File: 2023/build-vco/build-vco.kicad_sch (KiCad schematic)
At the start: 12 parts, among them M1 PMOS_OR1, M10 NMOS_OR1, M11 NMOS_OR1, M2 NMOS_OR1, M27 NMOS_OR1, M3 PMOS_OR1, M4 NMOS_OR1, M5 NMOS_OR1, M6 NMOS_OR1, M7 NMOS_OR1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

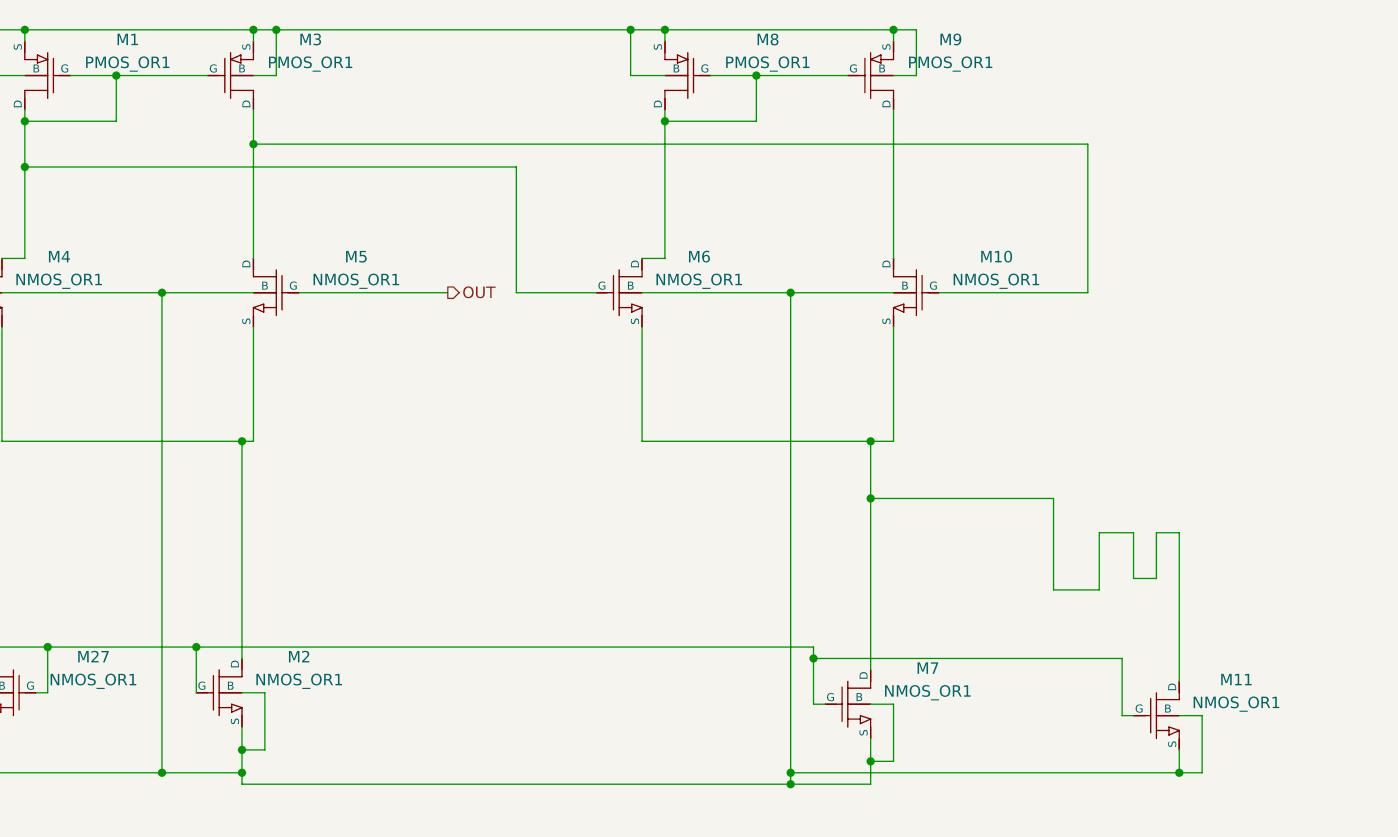
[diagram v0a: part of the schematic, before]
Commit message: DEBUG ポートを借り追加。LVS OK.
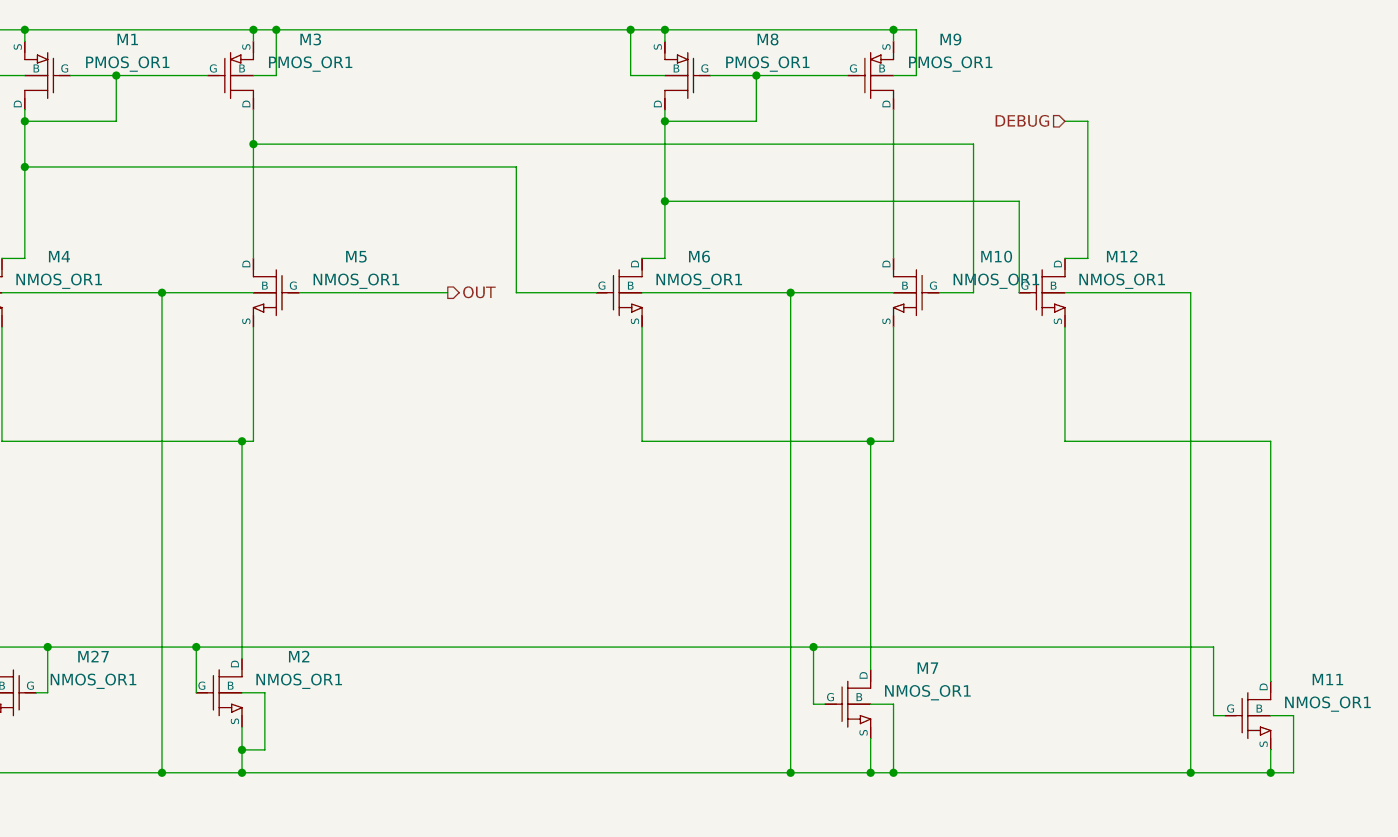
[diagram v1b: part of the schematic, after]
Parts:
- added M12: NMOS_OR1, symbol OR1Symbols:NMOS_OR1
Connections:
- net 0: now also M12.4 (B)
- net at M6.1 (D), M8.1 (D), M8.2 (G)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: now also M12.2 (G)
- net at M10.3 (S), M6.3 (S), M7.1 (D): no longer M11.1 (D)
- new net: M11.1 (D), M12.3 (S)
- new net DEBUG: M12.1 (D)
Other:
- moved on the sheet: M11

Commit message: 3段出来た。
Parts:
- added M13, M14: PMOS_OR1, symbol OR1Symbols:PMOS_OR1
- added M15: NMOS_OR1, symbol OR1Symbols:NMOS_OR1
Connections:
- net 0: now also M15.4 (B)
- net VDD: now also M13.3 (S), M13.4 (B), M14.3 (S), M14.4 (B)
- net at M10.1 (D), M9.1 (D): now also M15.2 (G)
- net at M11.1 (D), M12.3 (S): now also M15.3 (S)
- net DEBUG: no longer names the net of M12.1 (D)
- net DEBUG: now also M13.1 (D), M13.2 (G), M14.2 (G)
- new net: M14.1 (D), M15.1 (D)

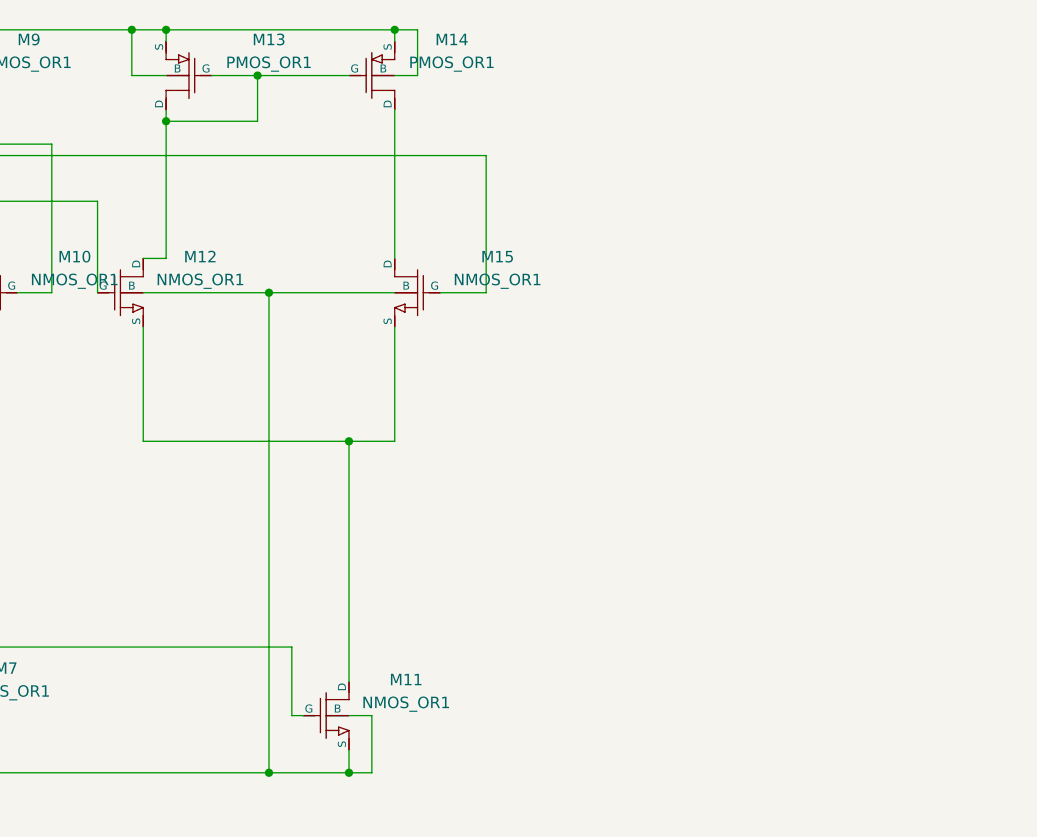
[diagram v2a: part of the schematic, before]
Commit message: 4段までOK. LVS OK.
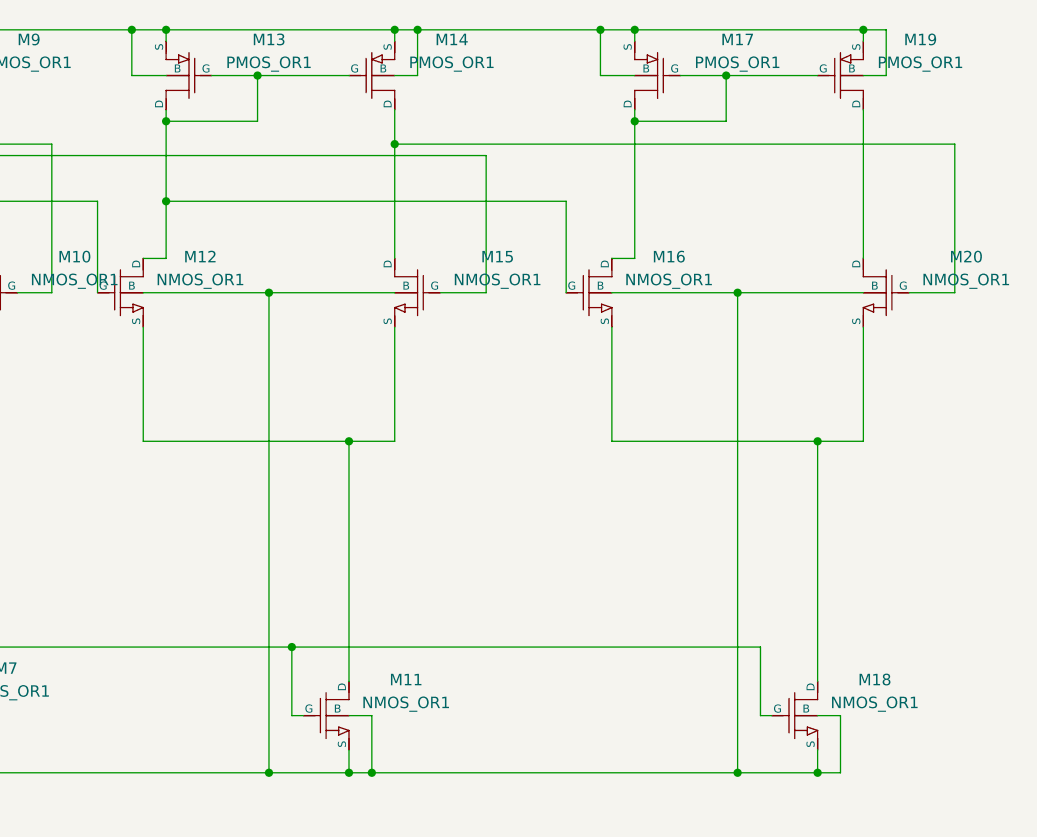
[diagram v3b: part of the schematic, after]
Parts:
- added M16, M18, M20: NMOS_OR1, symbol OR1Symbols:NMOS_OR1
- added M17, M19: PMOS_OR1, symbol OR1Symbols:PMOS_OR1
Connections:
- net 0: now also M16.4 (B), M18.3 (S), M18.4 (B), M20.4 (B)
- net IN: now also M18.2 (G)
- net VDD: now also M17.3 (S), M17.4 (B), M19.3 (S), M19.4 (B)
- net at M14.1 (D), M15.1 (D): now also M20.2 (G)
- net at M12.1 (D), M13.1 (D), M13.2 (G)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: now also M16.2 (G)
- new net: M16.1 (D), M17.1 (D), M17.2 (G), M19.2 (G)
- new net: M16.3 (S), M18.1 (D), M20.3 (S)
- new net: M19.1 (D), M20.1 (D)

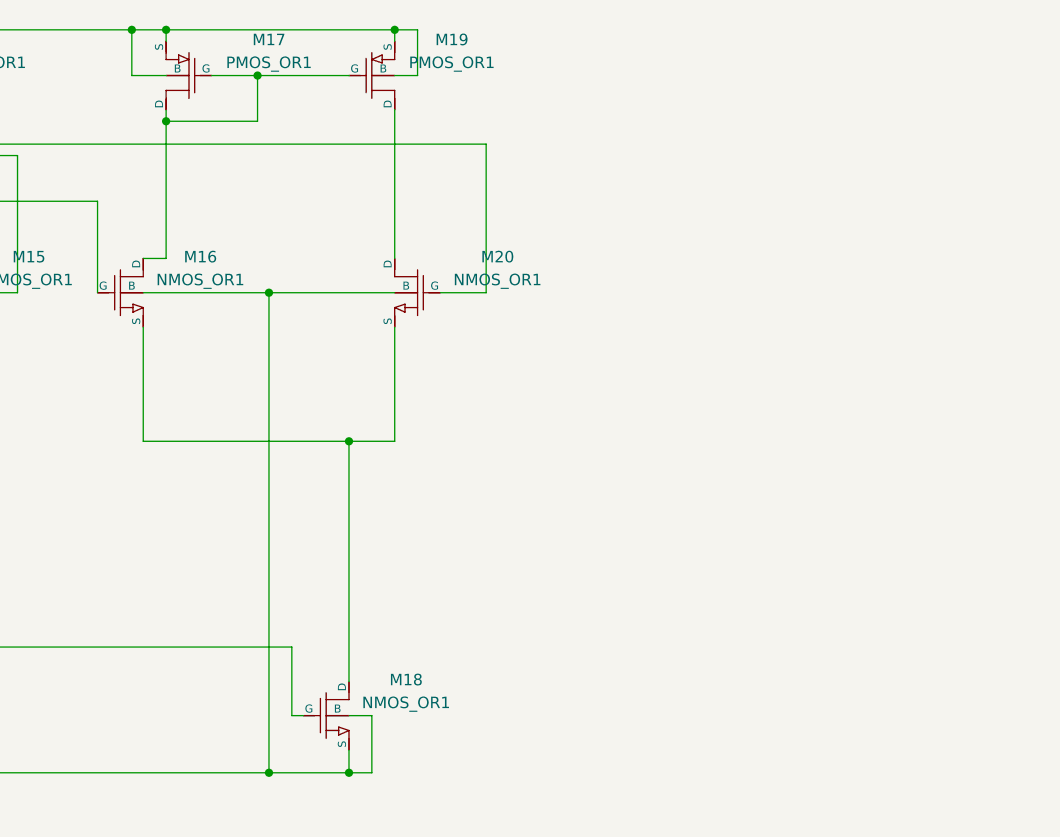
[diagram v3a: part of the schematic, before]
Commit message: 最終段の5段までOK. LVS OK.
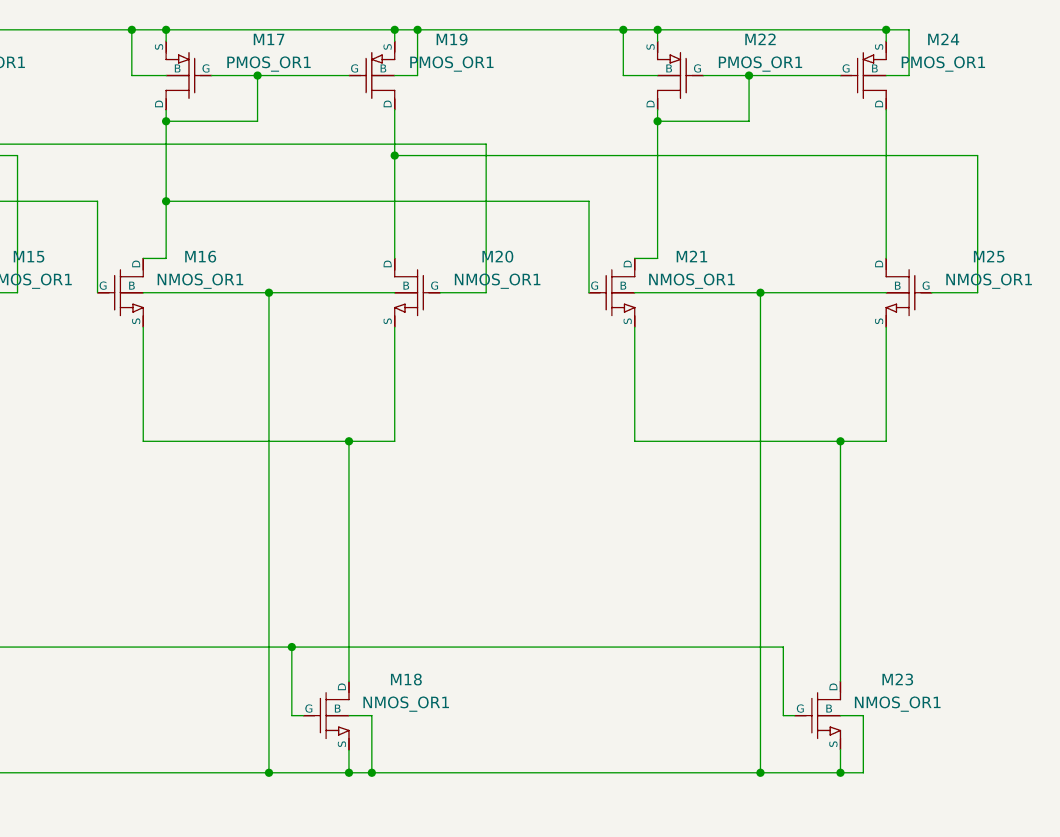
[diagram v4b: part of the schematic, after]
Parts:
- added M21, M23, M25: NMOS_OR1, symbol OR1Symbols:NMOS_OR1
- added M22, M24: PMOS_OR1, symbol OR1Symbols:PMOS_OR1
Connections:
- net 0: now also M21.4 (B), M23.3 (S), M23.4 (B), M25.4 (B)
- net IN: now also M23.2 (G)
- net VDD: now also M22.3 (S), M22.4 (B), M24.3 (S), M24.4 (B)
- net at M16.1 (D), M17.1 (D), M17.2 (G)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: now also M21.2 (G)
- net at M19.1 (D), M20.1 (D): now also M25.2 (G)
- new net: M24.1 (D), M25.1 (D)
- new net: M21.1 (D), M22.1 (D), M22.2 (G), M24.2 (G)
- new net: M21.3 (S), M23.1 (D), M25.3 (S)

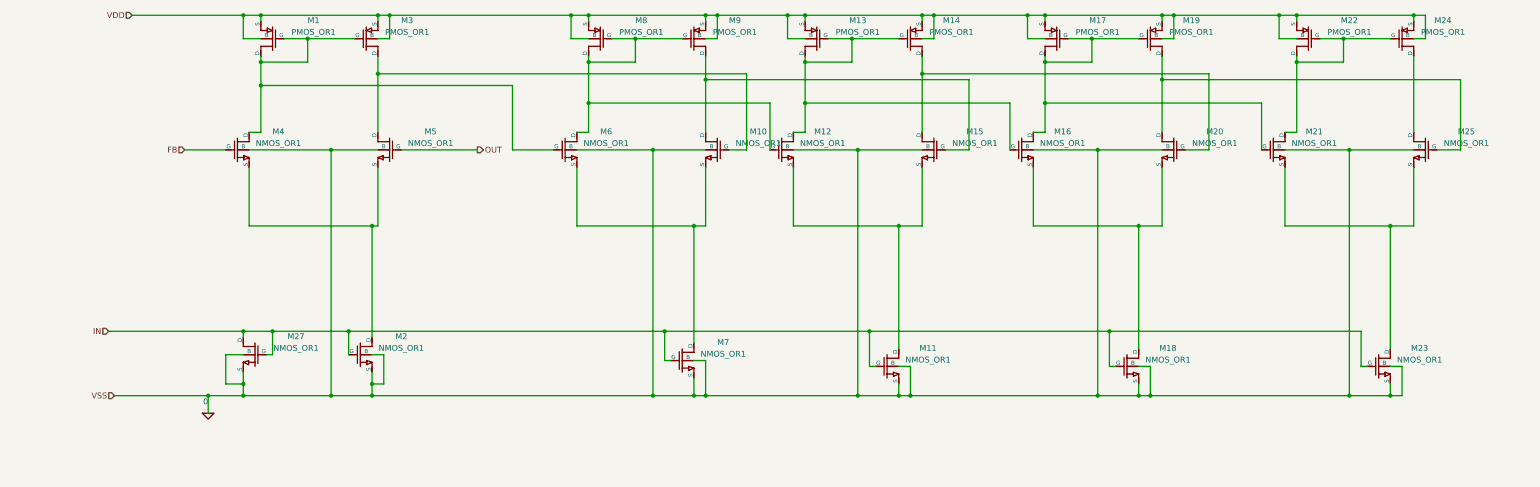
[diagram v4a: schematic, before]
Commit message: FB くっつけて LVS OK.
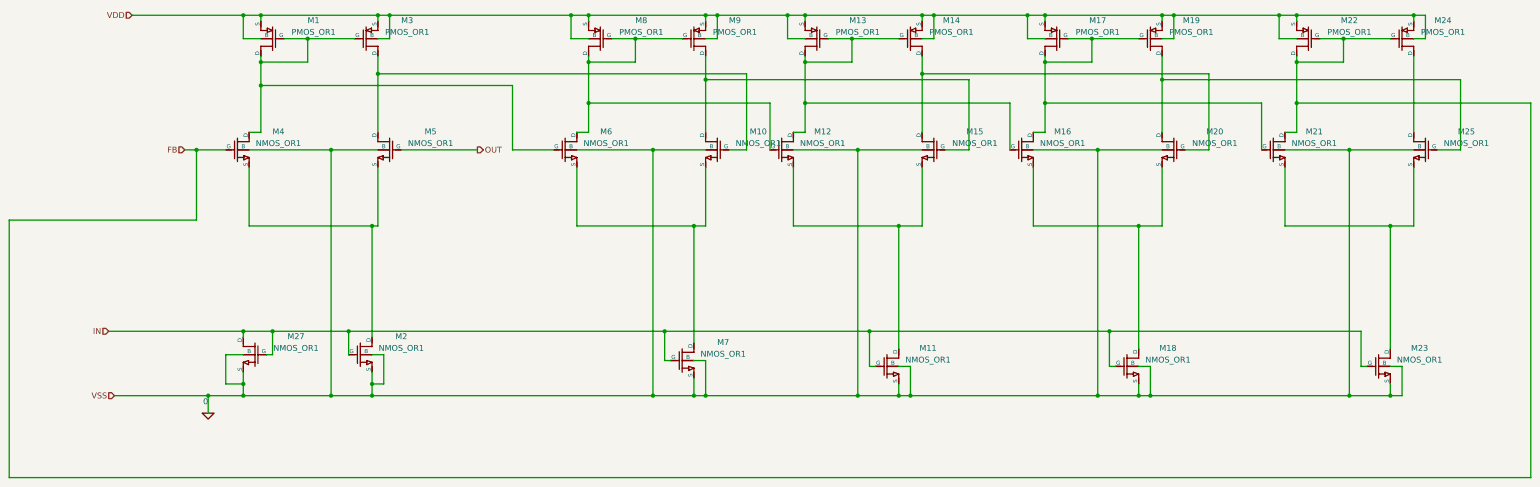
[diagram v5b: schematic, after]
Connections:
- net FB: now also M21.1 (D), M22.1 (D), M22.2 (G), M24.2 (G)
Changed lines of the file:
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@@
   (junction (at 142.24 132.08) (diameter 0) (color 0 0 0 0)
   )
+  (junction (at 40.64 92.71) (diameter 0) (color 0 0 0 0)
+  )
   (junction (at 279.4 73.66) (diameter 0) (color 0 0 0 0)
   )
@@
   (junction (at 151.13 63.5) (diameter 0) (color 0 0 0 0)
   )
+  (junction (at 279.4 82.55) (diameter 0) (color 0 0 0 0)
+  )
   (junction (at 245.11 109.22) (diameter 0) (color 0 0 0 0)
   )
@@
     (stroke (width 0) (type default))
   )
+  (wire (pts (xy 279.4 82.55) (xy 279.4 88.9))
+    (stroke (width 0) (type default))
+  )
   (wire (pts (xy 172.72 82.55) (xy 172.72 88.9))
     (stroke (width 0) (type default))
@@
     (stroke (width 0) (type default))
   )
+  (wire (pts (xy 330.2 82.55) (xy 330.2 163.83))
+    (stroke (width 0) (type default))
+  )
   (wire (pts (xy 250.19 63.5) (xy 252.73 63.5))
     (stroke (width 0) (type default))
@@
     (stroke (width 0) (type default))
   )
+  (wire (pts (xy 0 107.95) (xy 40.64 107.95))
+    (stroke (width 0) (type default))
+  )
   (wire (pts (xy 314.96 77.47) (xy 314.96 92.71))
     (stroke (width 0) (type default))
@@
     (stroke (width 0) (type default))
   )
-  (wire (pts (xy 279.4 73.66) (xy 279.4 88.9))
+  (wire (pts (xy 279.4 73.66) (xy 279.4 82.55))
     (stroke (width 0) (type default))
   )
@@
     (stroke (width 0) (type default))
   )
+  (wire (pts (xy 279.4 82.55) (xy 330.2 82.55))
+    (stroke (width 0) (type default))
+  )
   (wire (pts (xy 289.56 68.58) (xy 299.72 68.58))
     (stroke (width 0) (type default))
@@
     (stroke (width 0) (type default))
   )
-  (wire (pts (xy 38.1 92.71) (xy 46.99 92.71))
+  (wire (pts (xy 38.1 92.71) (xy 40.64 92.71))
     (stroke (width 0) (type default))
   )
@@
     (stroke (width 0) (type default))
   )
+  (wire (pts (xy 40.64 92.71) (xy 40.64 107.95))
+    (stroke (width 0) (type default))
+  )
   (wire (pts (xy 195.58 146.05) (xy 236.22 146.05))
     (stroke (width 0) (type default))
@@
     (stroke (width 0) (type default))
   )
+  (wire (pts (xy 330.2 163.83) (xy 0 163.83))
+    (stroke (width 0) (type default))
+  )
   (wire (pts (xy 245.11 109.22) (xy 245.11 135.89))
     (stroke (width 0) (type default))
@@
     (stroke (width 0) (type default))
   )
+  (wire (pts (xy 40.64 92.71) (xy 46.99 92.71))
+    (stroke (width 0) (type default))
+  )
   (wire (pts (xy 151.13 77.47) (xy 151.13 88.9))
     (stroke (width 0) (type default))
@@
     (stroke (width 0) (type default))
   )
+  (wire (pts (xy 0 163.83) (xy 0 107.95))
+    (stroke (width 0) (type default))
+  )
